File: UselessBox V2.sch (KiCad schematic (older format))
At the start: 21 parts, among them J2 Conn_01x03, J3 Conn_01x02_Female, SW1 SW_SPDT, SW2 SW_SPDT, U1 L7805CV, U2 LM555CN_NOPB

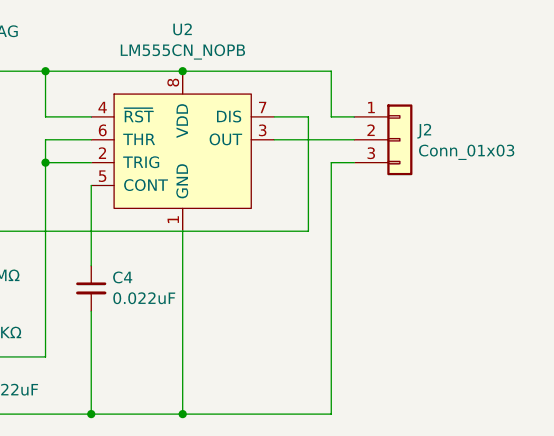
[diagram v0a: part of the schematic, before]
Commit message: corrected SERVO pinout
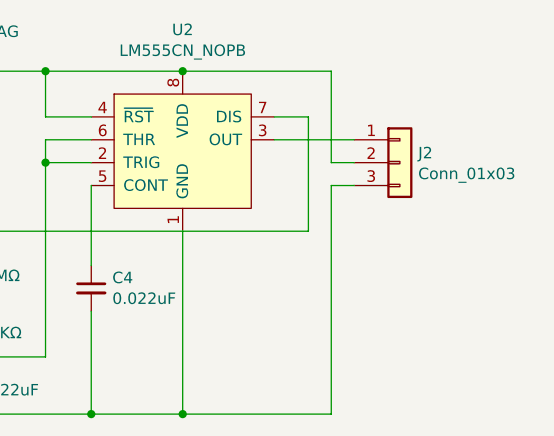
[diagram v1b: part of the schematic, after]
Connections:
- net 5Vout: now also J2.2 (Pin_2); no longer J2.1 (Pin_1)
- net at U2.3 (OUT): now also J2.1 (Pin_1); no longer J2.2 (Pin_2)
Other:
- moved on the sheet: J2
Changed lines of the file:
@@
 L Connector_Generic:Conn_01x03 J2
 U 1 1 6259A855
-P 9250 3150
-F 0 "J2" H 9330 3192 50  0000 L CNN
-F 1 "Conn_01x03" H 9330 3101 50  0000 L CNN
-F 2 "Connector_PinHeader_2.54mm:PinHeader_1x03_P2.54mm_Vertical" H 9250 3150 50  0001 C CNN
-F 3 "~" H 9250 3150 50  0001 C CNN
-	1    9250 3150
-	1    0    0    -1
-$EndComp
-Wire Wire Line
-	9050 3050 8950 3050
-Wire Wire Line
-	8950 3050 8950 2850
+P 9250 3250
+F 0 "J2" H 9330 3292 50  0000 L CNN
+F 1 "Conn_01x03" H 9330 3201 50  0000 L CNN
+F 2 "Connector_PinHeader_2.54mm:PinHeader_1x03_P2.54mm_Vertical" H 9250 3250 50  0001 C CNN
+F 3 "~" H 9250 3250 50  0001 C CNN
+	1    9250 3250
+	1    0    0    -1
+$EndComp
 Wire Wire Line
 	8950 2850 8300 2850
 Connection ~ 8300 2850
-Wire Wire Line
-	9050 3150 8700 3150
-Wire Wire Line
-	9050 3250 8950 3250
-Wire Wire Line
-	8950 3250 8950 4350
 Wire Wire Line
 	8950 4350 8300 4350
@@
 	3250 3650 3250 4050
 Connection ~ 3250 3650
+Wire Wire Line
+	8700 3150 9050 3150
+Wire Wire Line
+	9050 3250 8950 3250
+Wire Wire Line
+	8950 3250 8950 2850
+Wire Wire Line
+	9050 3350 8950 3350
+Wire Wire Line
+	8950 3350 8950 4350
 $EndSCHEMATC
